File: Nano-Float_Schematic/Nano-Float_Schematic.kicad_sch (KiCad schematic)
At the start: 8 parts, among them M1 Motor_DC, SW1 SW_DIP_x01, U1 MS5837-xxBA

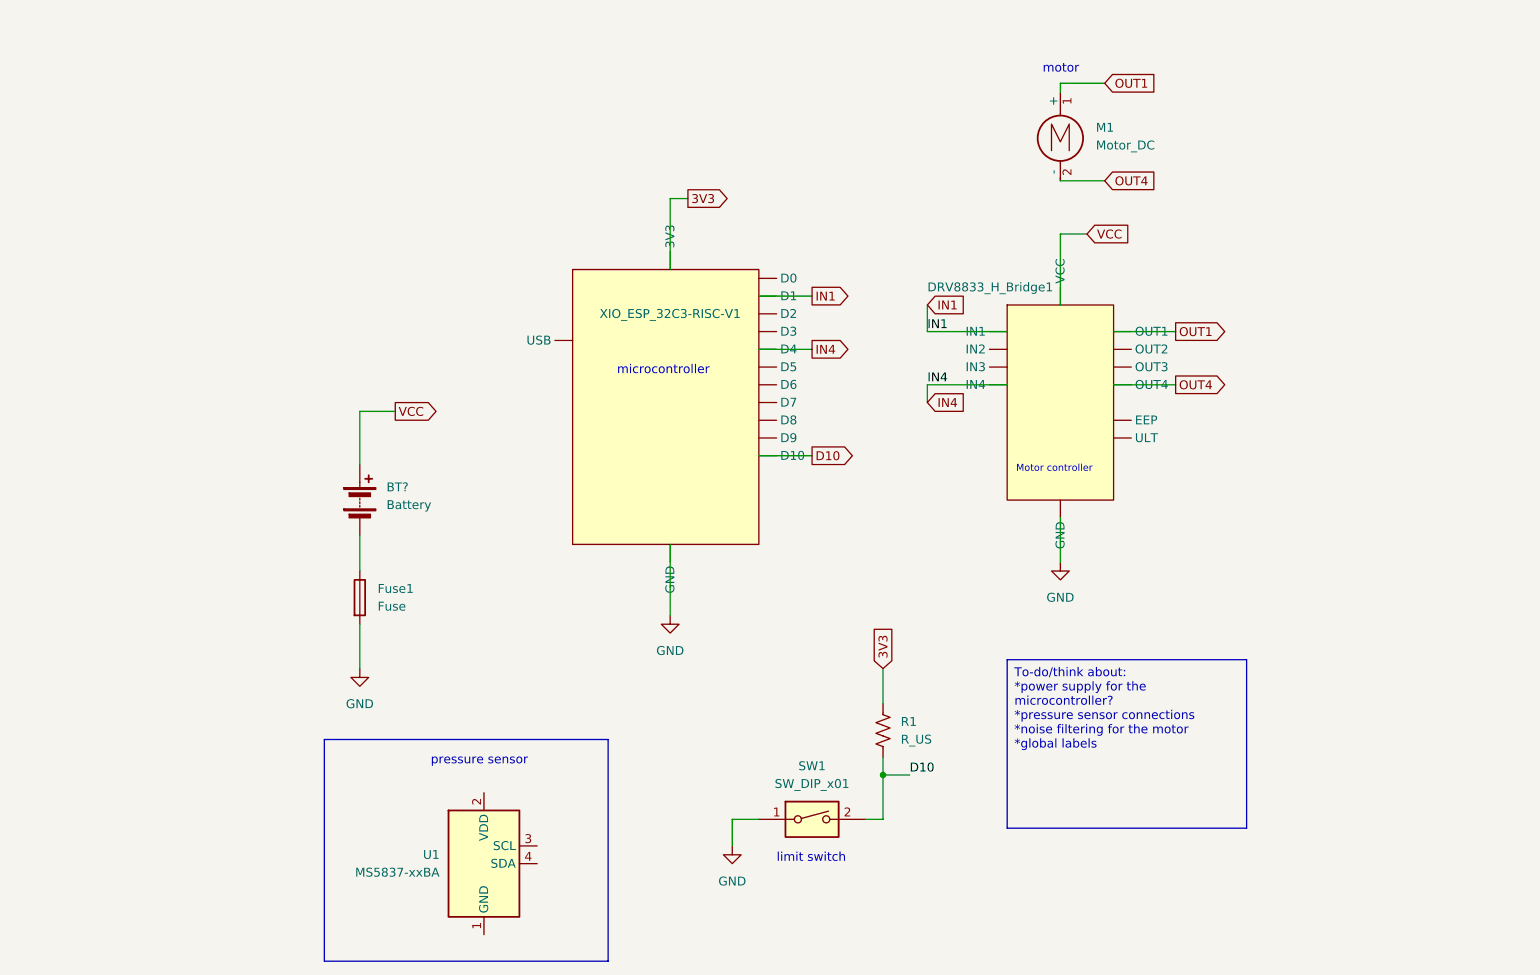
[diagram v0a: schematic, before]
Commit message: Update Nano-Float_Schematic.kicad_sch
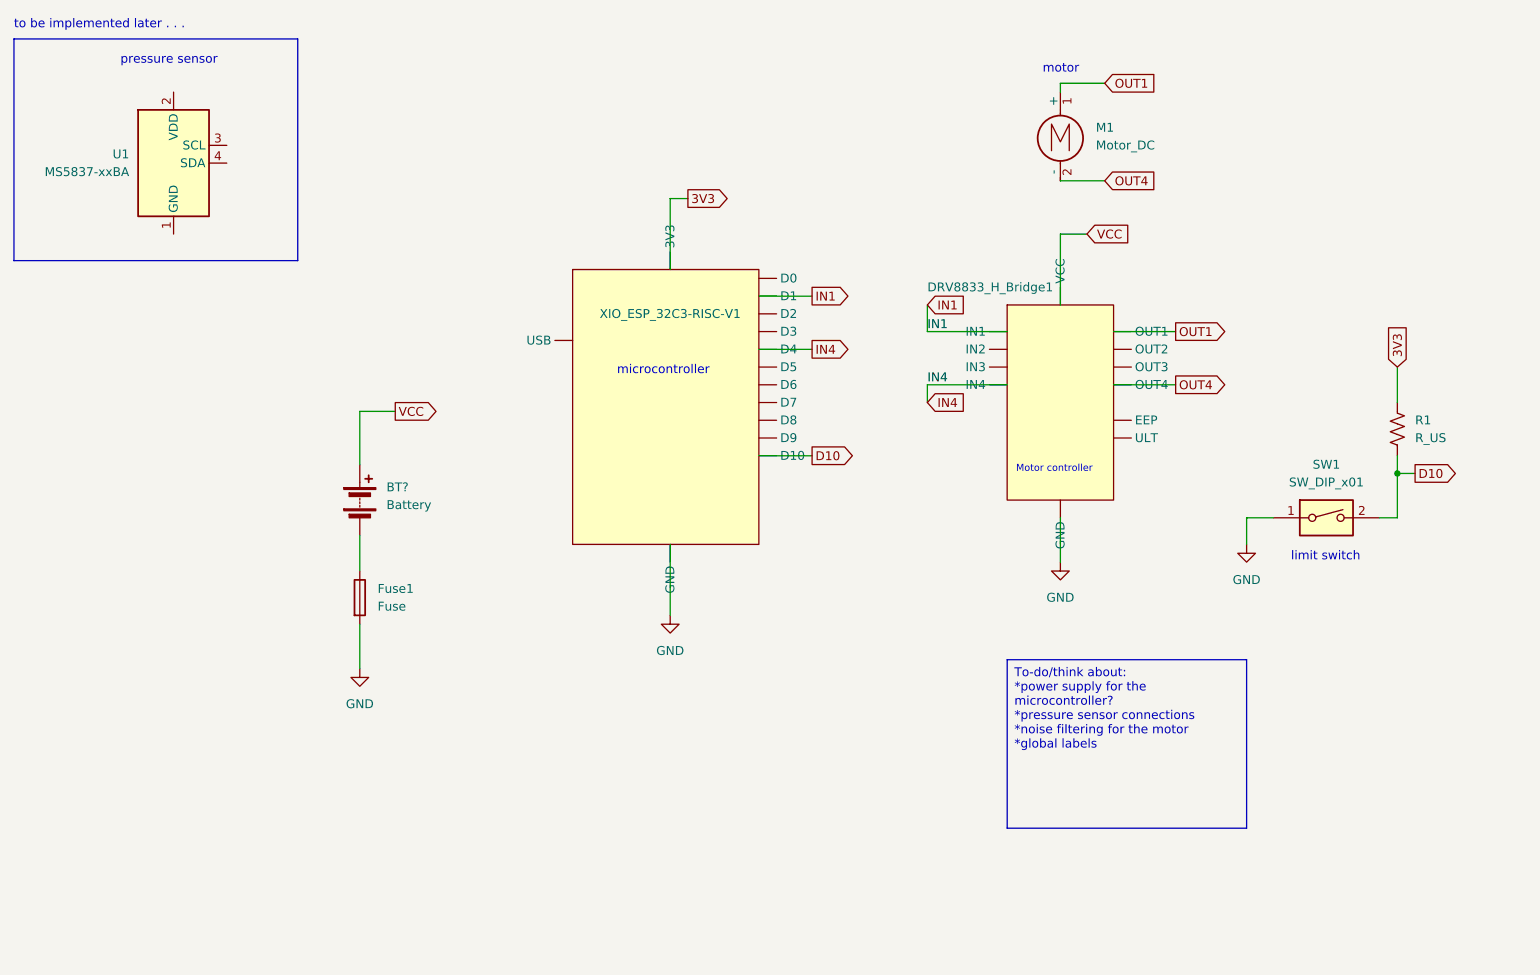
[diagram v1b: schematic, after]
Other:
- note added: "to be implemented later . . ."
- moved on the sheet: R1, SW1, U1
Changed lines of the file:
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@@
 (kicad_sch (version 20230121) (generator eeschema)
   (paper "A4")
-  (junction (at 144.78 147.32) (diameter 0) (color 0 0 0 0)
+  (junction (at 218.44 104.14) (diameter 0) (color 0 0 0 0)
   )
   (wire (pts (xy 116.84 64.77) (xy 114.3 64.77))
@@
     (stroke (width 0) (type default))
   )
-  (wire (pts (xy 144.78 132.08) (xy 144.78 137.16))
-    (stroke (width 0) (type default))
-  )
-  (wire (pts (xy 142.24 153.67) (xy 144.78 153.67))
+  (wire (pts (xy 218.44 88.9) (xy 218.44 93.98))
+    (stroke (width 0) (type default))
+  )
+  (wire (pts (xy 215.9 110.49) (xy 218.44 110.49))
     (stroke (width 0) (type default))
   )
@@
     (stroke (width 0) (type default))
   )
-  (wire (pts (xy 127 153.67) (xy 123.19 153.67))
+  (wire (pts (xy 200.66 110.49) (xy 196.85 110.49))
     (stroke (width 0) (type default))
   )
@@
     (stroke (width 0) (type default))
   )
-  (wire (pts (xy 123.19 153.67) (xy 123.19 157.48))
+  (wire (pts (xy 196.85 110.49) (xy 196.85 114.3))
     (stroke (width 0) (type default))
   )
@@
     (stroke (width 0) (type default))
   )
-  (wire (pts (xy 144.78 153.67) (xy 144.78 147.32))
+  (wire (pts (xy 218.44 110.49) (xy 218.44 104.14))
     (stroke (width 0) (type default))
   )
@@
     (stroke (width 0) (type default))
   )
-  (wire (pts (xy 144.78 147.32) (xy 144.78 144.78))
+  (wire (pts (xy 218.44 104.14) (xy 218.44 101.6))
     (stroke (width 0) (type default))
   )
@@
     (stroke (width 0) (type default))
   )
-  (wire (pts (xy 148.59 147.32) (xy 144.78 147.32))
-    (stroke (width 0) (type default))
-  )
-  (rectangle (start 64.77 142.24) (end 105.41 173.99)
+  (wire (pts (xy 218.44 104.14) (xy 220.98 104.14))
+    (stroke (width 0) (type default))
+  )
+  (rectangle (start 20.32 41.91) (end 60.96 73.66)
     (stroke (width 0) (type default))
     (fill (type none))
@@
     (effects (font (size 1 1)) (justify left bottom))
   )
-  (text "pressure sensor\n" (at 80.01 146.05 0)
-    (effects (font (size 1.27 1.27)) (justify left bottom))
-  )
-  (text "limit switch\n" (at 129.54 160.02 0)
+  (text "pressure sensor\n" (at 35.56 45.72 0)
+    (effects (font (size 1.27 1.27)) (justify left bottom))
+  )
+  (text "limit switch\n" (at 203.2 116.84 0)
     (effects (font (size 1.27 1.27)) (justify left bottom))
   )
@@
     (effects (font (size 1.27 1.27)) (justify left bottom))
   )
+  (text "to be implemented later . . . \n" (at 20.32 40.64 0)
+    (effects (font (size 1.27 1.27)) (justify left bottom))
+  )
   (text "microcontroller\n" (at 106.68 90.17 0)
     (effects (font (size 1.27 1.27)) (justify left bottom))
   )
-  (label "D10" (at 148.59 147.32 0) (fields_autoplaced)
-    (effects (font (size 1.27 1.27)) (justify left bottom))
-  )
   (label "IN1" (at 151.13 83.82 0) (fields_autoplaced)
     (effects (font (size 1.27 1.27)) (justify left bottom))
@@
     (effects (font (size 1.27 1.27)) (justify left bottom))
   )
+  (global_label "D10" (shape output) (at 220.98 104.14 0) (fields_autoplaced)
+    (effects (font (size 1.27 1.27)) (justify left))
+    (property "Intersheetrefs" "${INTERSHEET_REFS}" (at 227.6542 104.14 0)
+      (effects (font (size 1.27 1.27)) (justify left) hide)
+    )
+  )
   (global_label "OUT1" (shape input) (at 176.53 48.26 0) (fields_autoplaced)
     (effects (font (size 1.27 1.27)) (justify left))
@@
     )
   )
-  (global_label "3V3" (shape input) (at 144.78 132.08 90) (fields_autoplaced)
-    (effects (font (size 1.27 1.27)) (justify left))
-    (property "Intersheetrefs" "${INTERSHEET_REFS}" (at 144.78 125.5872 90)
+  (global_label "3V3" (shape input) (at 218.44 88.9 90) (fields_autoplaced)
+    (effects (font (size 1.27 1.27)) (justify left))
+    (property "Intersheetrefs" "${INTERSHEET_REFS}" (at 218.44 82.4072 90)
       (effects (font (size 1.27 1.27)) (justify left) hide)
     )
@@
     )
   )
-  (symbol (lib_id "Sensor_Pressure:MS5837-xxBA") (at 87.63 160.02 0) (unit 1)
-    (in_bom yes) (on_board yes) (dnp no) (fields_autoplaced)
-    (property "Reference" "U1" (at 81.28 158.75 0)
+  (symbol (lib_id "Sensor_Pressure:MS5837-xxBA") (at 43.18 59.69 0) (unit 1)
+    (in_bom yes) (on_board yes) (dnp no) (fields_autoplaced)
+    (property "Reference" "U1" (at 36.83 58.42 0)
       (effects (font (size 1.27 1.27)) (justify right))
     )
-    (property "Value" "MS5837-xxBA" (at 81.28 161.29 0)
+    (property "Value" "MS5837-xxBA" (at 36.83 60.96 0)
       (effects (font (size 1.27 1.27)) (justify right))
     )
-    (property "Footprint" "Sensor_Pressure:TE_MS5837-xxBA" (at 87.63 160.02 0)
-      (effects (font (size 1.27 1.27)) hide)
-    )
-    (property "Datasheet" "https://www.te.com/commerce/DocumentDelivery/DDEController?Action=showdoc&DocId=Data+Sheet%7FMS5837-30BA%7FB1%7Fpdf%7FEnglish%7FENG_DS_MS5837-30BA_B1.pdf%7FCAT-BLPS0017" (at 87.63 162.56 0)
+    (property "Footprint" "Sensor_Pressure:TE_MS5837-xxBA" (at 43.18 59.69 0)
+      (effects (font (size 1.27 1.27)) hide)
+    )
+    (property "Datasheet" "https://www.te.com/commerce/DocumentDelivery/DDEController?Action=showdoc&DocId=Data+Sheet%7FMS5837-30BA%7FB1%7Fpdf%7FEnglish%7FENG_DS_MS5837-30BA_B1.pdf%7FCAT-BLPS0017" (at 43.18 62.23 0)
       (effects (font (size 1.27 1.27)) hide)
     )
@@
     )
   )
-  (symbol (lib_id "Switch:SW_DIP_x01") (at 134.62 153.67 0) (unit 1)
-    (in_bom yes) (on_board yes) (dnp no) (fields_autoplaced)
-    (property "Reference" "SW1" (at 134.62 146.05 0)
-      (effects (font (size 1.27 1.27)))
-    )
-    (property "Value" "SW_DIP_x01" (at 134.62 148.59 0)
-      (effects (font (size 1.27 1.27)))
-    )
-    (property "Footprint" "" (at 134.62 153.67 0)
-      (effects (font (size 1.27 1.27)) hide)
-    )
-    (property "Datasheet" "~" (at 134.62 153.67 0)
+  (symbol (lib_id "Switch:SW_DIP_x01") (at 208.28 110.49 0) (unit 1)
+    (in_bom yes) (on_board yes) (dnp no) (fields_autoplaced)
+    (property "Reference" "SW1" (at 208.28 102.87 0)
+      (effects (font (size 1.27 1.27)))
+    )
+    (property "Value" "SW_DIP_x01" (at 208.28 105.41 0)
+      (effects (font (size 1.27 1.27)))
+    )
+    (property "Footprint" "" (at 208.28 110.49 0)
+      (effects (font (size 1.27 1.27)) hide)
+    )
+    (property "Datasheet" "~" (at 208.28 110.49 0)
       (effects (font (size 1.27 1.27)) hide)
     )
@@
     )
   )
-  (symbol (lib_id "power:GND") (at 123.19 157.48 0) (unit 1)
-    (in_bom yes) (on_board yes) (dnp no) (fields_autoplaced)
-    (property "Reference" "#PWR02" (at 123.19 163.83 0)
-      (effects (font (size 1.27 1.27)) hide)
-    )
-    (property "Value" "GND" (at 123.19 162.56 0)
-      (effects (font (size 1.27 1.27)))
-    )
-    (property "Footprint" "" (at 123.19 157.48 0)
-      (effects (font (size 1.27 1.27)) hide)
-    )
-    (property "Datasheet" "" (at 123.19 157.48 0)
+  (symbol (lib_id "power:GND") (at 196.85 114.3 0) (unit 1)
+    (in_bom yes) (on_board yes) (dnp no) (fields_autoplaced)
+    (property "Reference" "#PWR02" (at 196.85 120.65 0)
+      (effects (font (size 1.27 1.27)) hide)
+    )
+    (property "Value" "GND" (at 196.85 119.38 0)
+      (effects (font (size 1.27 1.27)))
+    )
+    (property "Footprint" "" (at 196.85 114.3 0)
+      (effects (font (size 1.27 1.27)) hide)
+    )
+    (property "Datasheet" "" (at 196.85 114.3 0)
       (effects (font (size 1.27 1.27)) hide)
     )
@@
     )
   )
-  (symbol (lib_id "Device:R_US") (at 144.78 140.97 0) (unit 1)
-    (in_bom yes) (on_board yes) (dnp no) (fields_autoplaced)
-    (property "Reference" "R1" (at 147.32 139.7 0)
-      (effects (font (size 1.27 1.27)) (justify left))
-    )
-    (property "Value" "R_US" (at 147.32 142.24 0)
-      (effects (font (size 1.27 1.27)) (justify left))
-    )
-    (property "Footprint" "Resistor_THT:R_Radial_Power_L7.0mm_W8.0mm_Px2.40mm_Py2.30mm" (at 145.796 141.224 90)
-      (effects (font (size 1.27 1.27)) hide)
-    )
-    (property "Datasheet" "~" (at 144.78 140.97 0)
-      (effects (font (size 1.27 1.27)) hide)
-    )
+  (symbol (lib_id "Device:R_US") (at 218.44 97.79 0) (unit 1)
+    (in_bom yes) (on_board yes) (dnp no) (fields_autoplaced)
+    (property "Reference" "R1" (at 220.98 96.52 0)
+      (effects (font (size 1.27 1.27)) (justify left))
+    )
+    (property "Value" "R_US" (at 220.98 99.06 0)
+      (effects (font (size 1.27 1.27)) (justify left))
+    )
+    (property "Footprint" "Resistor_THT:R_Radial_Power_L7.0mm_W8.0mm_Px2.40mm_Py2.30mm" (at 219.456 98.044 90)
+      (effects (font (size 1.27 1.27)) hide)
+    )
+    (property "Datasheet" "~" (at 218.44 97.79 0)
+      (effects (font (size 1.27 1.27)) hide)
+    )

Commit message: Got the Footprints! Need to play around more with the orientation of everything on the final PCB
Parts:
- removed XIO_ESP_32C3-RISC-V1: ~, symbol Nano-Flat Schematic Library:XIAO_ESP_32C3-RISC-V
- added XIAO_ESP_32C3-RISC-V1: ~, Nano-Float_Schematic:MODULE_102010388, symbol Nano-Flat Schematic Library:XIAO_ESP_32C3-RISC-V
- BT1: renamed from BT?; footprint (none) -> Battery:Battery_Panasonic_CR1025-VSK_Vertical_CircularHoles
- DRV8833_H_Bridge1: footprint (none) -> Nano-Float_Schematic:SOT5X3-6_DRL_TEX
- Fuse1: footprint Fuse:Fuse_0402_1005Metric_Pad0.77x0.64mm_HandSolder -> Fuse:Fuseholder_Blade_ATO_Littelfuse_Pudenz_2_Pin
- M1: footprint (none) -> Connector_PinHeader_2.54mm:PinHeader_2x01_P2.54mm_Vertical
- R1: footprint Resistor_THT:R_Radial_Power_L7.0mm_W8.0mm_Px2.40mm_Py2.30mm -> Resistor_THT:R_Axial_DIN0207_L6.3mm_D2.5mm_P10.16mm_Horizontal
- SW1: footprint (none) -> Nano-Float_Schematic:SW_ESE-22MV21T
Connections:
- net 3V3: now also XIAO_ESP_32C3-RISC-V1. (USB)
- net D10: now also XIAO_ESP_32C3-RISC-V1. (USB)
- net GND: now also XIAO_ESP_32C3-RISC-V1. (USB)
- net IN1: now also XIAO_ESP_32C3-RISC-V1. (USB)
- net IN4: now also XIAO_ESP_32C3-RISC-V1. (USB)
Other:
- note added: "goes to pressure sensor"
- moved on the sheet: U1
